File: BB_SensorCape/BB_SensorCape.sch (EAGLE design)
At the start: 15 parts, among them U1 FGPMMOPA6H

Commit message: schematic updates 12/23
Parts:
- removed B1: CR1220, microbuilder:BATTERYCR1220_SMT
- added C2: 0.1uF, SparkFun-Capacitors:0.1UF-25V-5%(0603)
- added C5, C6, C7, C8, C9: 0.1 uF, SparkFun-Capacitors:CAP0805
- added JP1: M02PTH, SparkFun-Connectors:M02PTH
- added JP2, JP3: (no value), adafruit:PINHD-2X4
- added PCB1: BEAGLEBONE_BLACK, e14_BeagleBoneBlack_RevA:BEAGLEBONE_BLACK
- added R10, R11, R12: 4.75K, resistor:R-US_R0603
- added R13: 10K, resistor:R-US_R0603
- added R14, R15, R5, R9: 5.6K, resistor:R-US_R0603
- added SW1: (no value), SparkFun-Electromechanical:SW_DIP-2-SMT-HALFSIZE
- added U$9: ISL29125, SparkFun-Sensors:ISL29125
- added U2: MAX232SOIC16, SparkFun-DigitalIC:MAX232SOIC16
- added X1: (no value), SparkFun-Connectors:DB9MALE
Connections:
- removed net I2C_SCL: R3.1, U$1.I2C1_SCL
- removed net I2C_SDA: R4.1, U$1.I2C1_SDA
- removed net VBACKUP: B1.+, U1.VBACKUP
- new net BB_GPS_RX: JP2.7, U$1.UART1_RXD
- new net BB_GPS_TX: JP2.3, U$1.UART1_TXD
- new net DBG_RX: U$1.UART2_RXD
- new net DBG_TX: U$1.UART2_TXD
- new net I2C2_SCL: R3.1, R5.1, U$1.I2C2_SCL, U$4.SCL
- new net I2C2_SDA: R4.1, R9.1, U$1.I2C2_SDA, U$4.SDA
- new net N$10: C7.1, U2.V-
- new net N$11: R11.1, SW1.1, U$4.A1
- new net N$12: R10.1, U$4.A2
- new net N$13: JP1.2, R13.1, U$4.WP
- new net N$14: C5.2, U2.C1-
- new net N$23: C8.1, U2.V+
- new net N$24: C5.1, U2.C1+
- new net N$27: C6.1, U2.C2+
- new net N$28: C6.2, U2.C2-
- new net N$9: R12.1, SW1.2, U$4.A0
- new net RXD: JP2.1, U2.R1OUT
- new net RXD#: U2.R1IN, X1.3
- new net TXD: JP2.5, U2.T1IN
- new net TXD#: U2.T1OUT, X1.2
- net 3.3V: now also C2.1, C9.1, R10.2, R11.2, R12.2, R5.2, R9.2, U$4.VCC, U2.VCC
- net GND: now also C2.2, C7.2, C8.2, C9.2, JP1.1, SW1.3, SW1.4, U$4.GND, U2.GND, U2.R2IN, U2.T2IN, X1.5; no longer B1.-
- net GPS_RX: now also JP2.2, JP2.4, U1.RX; no longer U$1.UART1_RXD, U1.TX
- net GPS_TX: now also JP2.6, JP2.8, U1.TX; no longer U$1.UART1_TXD, U1.RX
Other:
- note added: "Board Dimensions: 0.6" x 0.8""
- note added: "Board Dimensions: 1.5" x 0.9""
- note added: "I2C Address Range: 0x54 - 0x57"
- note added: "I2C Address: 0x44"
- note added: "Pin compatible with MAX3232E (3.3V Part)."
- note added: "Set Jumpers 1-2 and 5-6 for Serial Port-to-GPS Set Jumpers 3-4 and 7-8 for Beaglebone-to-GPS"
- note added: "Set Jumpers 3-4 and 7-8 for Beaglebone-to-Serial Port Only Install if Jumpers 3-4 and 7-8 are set on JP2"
- note added: "Shunt jumper enables EEPROM write."
- note added: "Use Digikey Part No. A35105-ND (Male Version) Confirm PCB footprint is for female (pins will need to be reversed on schematic if that's the case)"
- note added: "VERIFY SERIAL PORT JUMPER WIRING"
- note removed: "ADD SERIAL PORT COM"
- moved on the sheet: C1, LED2, R1, R2, R3, R4, R6, R7, R8, U$1, U$2, U$4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

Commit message: updates 12/24
added ISL29125 and started PWB design for area study
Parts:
- added C3: 1uF, SparkFun-Capacitors:CAP0805
- added C4: 0.1uF, SparkFun-Capacitors:0.1UF-25V-5%(0603)
- added R16: 10K, resistor:R-US_R0603
- added R17: 100, resistor:R-US_R0603
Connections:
- removed net FIX: LED2.A, U1.3D-FIX
- new net GPS_FIX: LED2.A, U$1.GPIO2_6, U1.3D-FIX
- new net ISL29125_INT: R16.1, U$1.GPIO2_9, U$9.!INT
- new net N$15: R14.1, U$9.SDA
- new net N$16: R15.1, U$9.SCL
- new net N$18: C3.1, C4.1, R17.1, U$9.VDD
- net 3.3V: now also PCB1.P9.3, PCB1.P9.4, R14.2, R15.2, R16.2, R17.2
- net 5V: now also PCB1.P9.5, PCB1.P9.6
- net DBG_RX: now also JP3.7
- net DBG_TX: now also JP3.3
- net GND: now also C3.2, C4.2, PCB1.P8.1, PCB1.P8.2, PCB1.P9.1, PCB1.P9.2, PCB1.P9.43, PCB1.P9.44, PCB1.P9.45, PCB1.P9.46, U$9.GND
- net RXD: now also JP3.8
- net TXD: now also JP3.4
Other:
- note added: "CALCULATE TOTAL CURRENT DRAW"
- note added: "I2C Addresses: 0x19, 0x1E, 0x6B, and 0x77"
- note removed: "ADD AMBIENT LIGHT SENSOR"
- note removed: "Wire FIX to GPIO?"
- moved on the sheet: C5, C6, C7, C8, C9, JP2, JP3, U2, X1

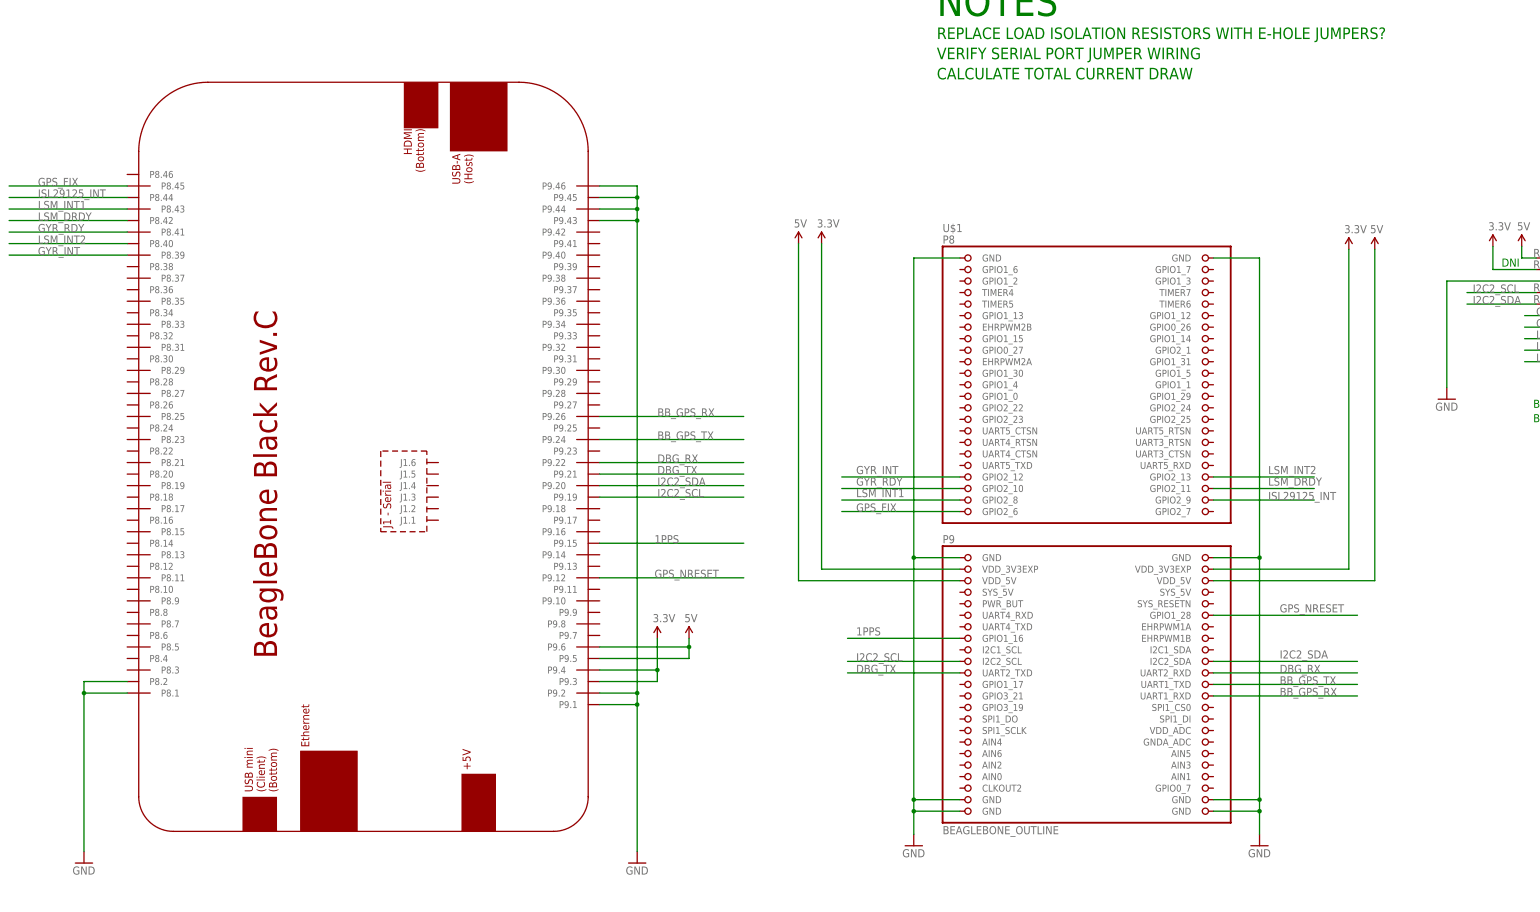
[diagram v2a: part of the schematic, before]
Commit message: Schematic/Board updates 01/03
Minor updates over holiday break
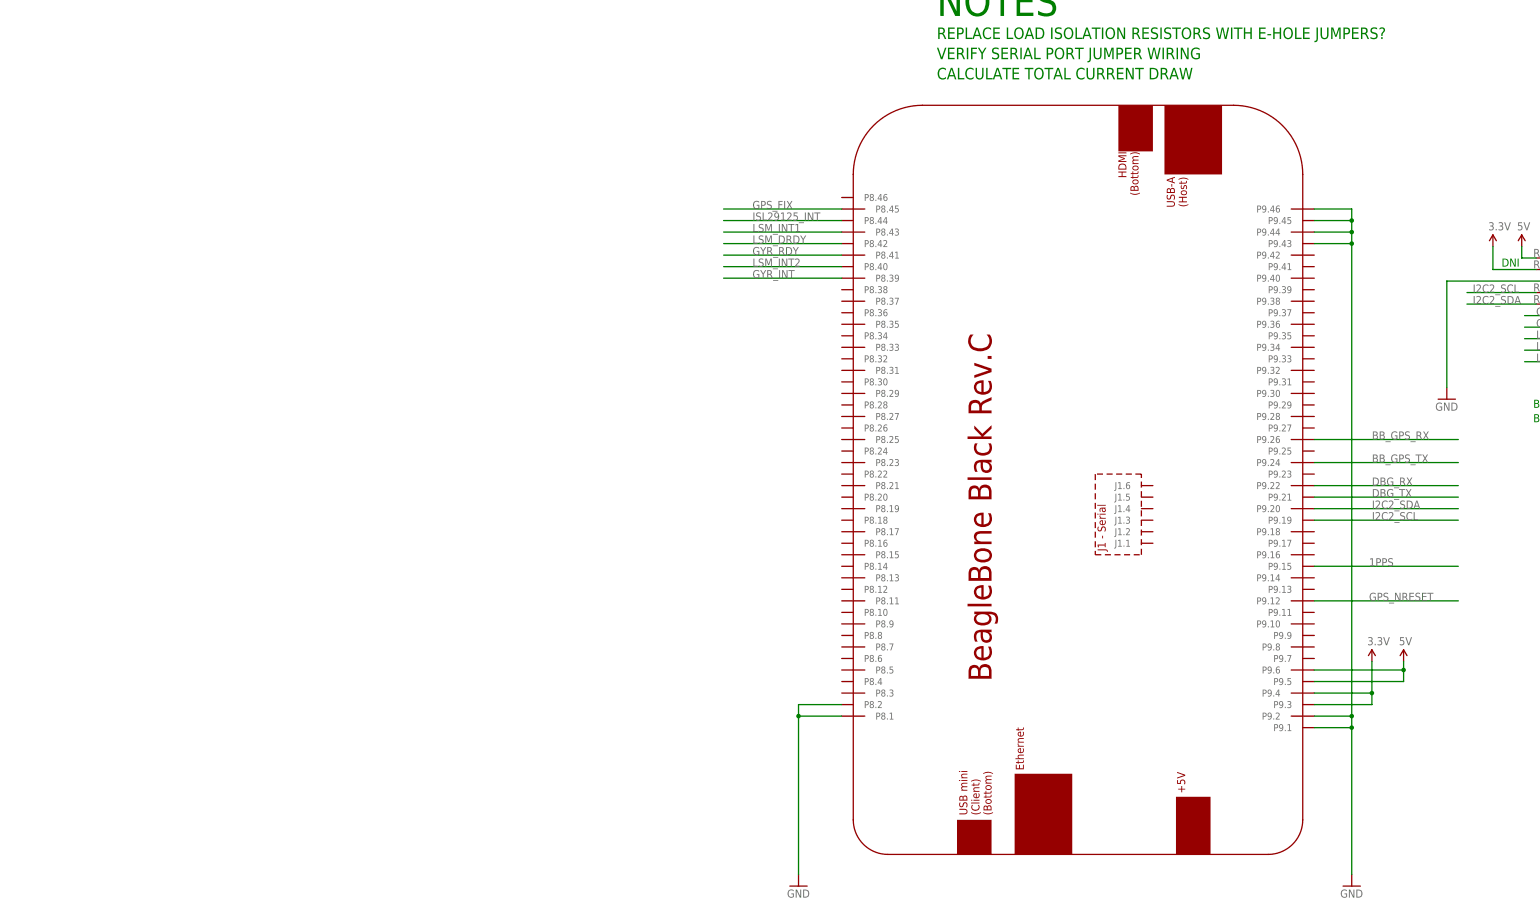
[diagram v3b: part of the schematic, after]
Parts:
- removed U$1: BEAGLEBONE_OUTLINE, adafruit:BEAGLEBONE_OUTLINE
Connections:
- net 1PPS: now also PCB1.P9.15; no longer U$1.GPIO1_16
- net 3.3V: no longer U$1.VDD_3V3EXP@1, U$1.VDD_3V3EXP@2
- net 5V: no longer U$1.VDD_5V@1, U$1.VDD_5V@2
- net BB_GPS_RX: now also PCB1.P9.26; no longer U$1.UART1_RXD
- net BB_GPS_TX: now also PCB1.P9.24; no longer U$1.UART1_TXD
- net DBG_RX: now also PCB1.P9.22; no longer U$1.UART2_RXD
- net DBG_TX: now also PCB1.P9.21; no longer U$1.UART2_TXD
- net GND: no longer U$1.GND@1, U$1.GND@2, U$1.GND@3, U$1.GND@4, U$1.GND@5, U$1.GND@6, U$1.GND@7, U$1.GND@8
- net GPS_FIX: now also PCB1.P8.45; no longer U$1.GPIO2_6
- net GPS_NRESET: now also PCB1.P9.12; no longer U$1.GPIO1_28
- net GYR_INT: now also PCB1.P8.39; no longer U$1.GPIO2_12
- net GYR_RDY: now also PCB1.P8.41; no longer U$1.GPIO2_10
- net I2C2_SCL: now also PCB1.P9.19; no longer U$1.I2C2_SCL
- net I2C2_SDA: now also PCB1.P9.20; no longer U$1.I2C2_SDA
- net ISL29125_INT: now also PCB1.P8.44; no longer U$1.GPIO2_9
- net LSM_DRDY: now also PCB1.P8.42; no longer U$1.GPIO2_11
- net LSM_INT1: now also PCB1.P8.43; no longer U$1.GPIO2_8
- net LSM_INT2: now also PCB1.P8.40; no longer U$1.GPIO2_13

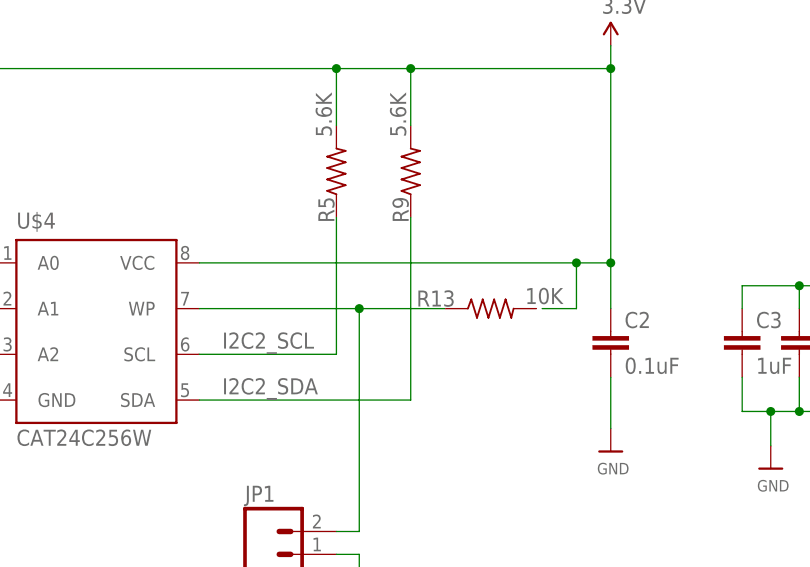
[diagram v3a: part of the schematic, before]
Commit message: Board updates 01/04
routing at ~98%
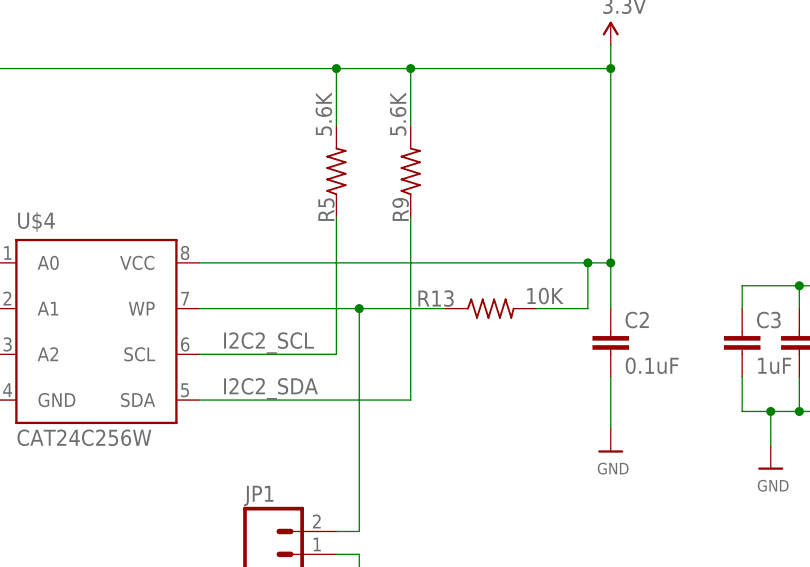
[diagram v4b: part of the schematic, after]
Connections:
- net 3.3V: now also R13.2
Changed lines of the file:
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@@
 <setting verticaltext="up"/>
 </settings>
-<grid distance="0.1" unitdist="inch" unit="inch" style="lines" multiple="1" display="no" altdistance="0.01" altunitdist="inch" altunit="inch"/>
+<grid distance="0.1" unitdist="inch" unit="inch" style="lines" multiple="1" display="yes" altdistance="0.01" altunitdist="inch" altunit="inch"/>
 <layers>
 <layer number="1" name="Top" color="4" fill="1" visible="no" active="no"/>
@@
 <wire x1="363.22" y1="127" x2="363.22" y2="132.08" width="0.1524" layer="91"/>
 <pinref part="U$4" gate="G$1" pin="VCC"/>
-<wire x1="363.22" y1="132.08" x2="359.41" y2="132.08" width="0.1524" layer="91"/>
 <pinref part="SUPPLY8" gate="G$1" pin="3.3V"/>
-<wire x1="359.41" y1="132.08" x2="317.5" y2="132.08" width="0.1524" layer="91"/>
+<wire x1="363.22" y1="132.08" x2="360.68" y2="132.08" width="0.1524" layer="91"/>
+<wire x1="360.68" y1="132.08" x2="317.5" y2="132.08" width="0.1524" layer="91"/>
 <wire x1="363.22" y1="132.08" x2="363.22" y2="153.67" width="0.1524" layer="91"/>
 <junction x="363.22" y="132.08"/>
@@
 <wire x1="277.495" y1="153.67" x2="283.21" y2="153.67" width="0.1524" layer="91"/>
 <junction x="283.21" y="153.67"/>
-<wire x1="355.6" y1="127" x2="359.41" y2="127" width="0.1524" layer="91"/>
-<wire x1="359.41" y1="127" x2="359.41" y2="132.08" width="0.1524" layer="91"/>
-<junction x="359.41" y="132.08"/>
+<wire x1="360.68" y1="132.08" x2="360.68" y2="127" width="0.1524" layer="91"/>
+<junction x="360.68" y="132.08"/>
+<wire x1="360.68" y1="127" x2="354.965" y2="127" width="0.1524" layer="91"/>
+<pinref part="R13" gate="G$1" pin="2"/>
 </segment>
 <segment>

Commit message: Schematic changes 02/03
Moved to FTDI interface for serial console
Refined jumper selection for serial console
Using TSL2561 BoB for ambient light sensor
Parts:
- removed C3: 1uF, SparkFun-Capacitors:CAP0805
- removed C4: 0.1uF, SparkFun-Capacitors:0.1UF-25V-5%(0603)
- removed C5, C6, C7, C8, C9: 0.1 uF, SparkFun-Capacitors:CAP0805
- removed U$9: ISL29125, SparkFun-Sensors:ISL29125
- removed U2: MAX232SOIC16, SparkFun-DigitalIC:MAX232SOIC16
- removed X1: (no value), SparkFun-Connectors:DB9MALE
- added JP4: FTDI_BASICPTH, SparkFun-Connectors:FTDI_BASICPTH
- added JP5: (no value), SparkFun-Connectors:M07
- added R18, R19: 4.75K, resistor:R-US_R0603
- added R20, R21: 0, resistor:R-US_R0603
- JP2: device adafruit:PINHD-2X4 -> jumper:JP4Q
- JP3: device adafruit:PINHD-2X4 -> jumper:JP2Q
- R14: value 5.6K -> 10K
- R15: value 5.6K -> 1K
- R16: value 10K -> 1K
- R17: value 100 -> 0
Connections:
- removed net N$18: C3.1, C4.1, R17.1, U$9.VDD
- removed net N$23: C8.1, U2.V+
- removed net N$24: C5.1, U2.C1+
- removed net N$27: C6.1, U2.C2+
- removed net N$28: C6.2, U2.C2-
- removed net RXD: JP2.1, JP3.8, U2.R1OUT
- removed net RXD#: U2.R1IN, X1.3
- removed net TXD: JP2.5, JP3.4, U2.T1IN
- removed net TXD#: U2.T1OUT, X1.2
- new net FTDI_RXD: JP2.2, JP3.3, JP4.2
- new net FTDI_TXD: JP2.6, JP3.1, JP4.3
- new net TSL2561_INT: JP5.5, PCB1.P8.46, R14.1
- net 3.3V: now also JP5.3, R18.2, R19.2, R21.2; no longer C9.1, R15.2, R17.2, U2.VCC
- net BB_GPS_RX: now also JP2.4, R18.1; no longer JP2.7
- net BB_GPS_TX: now also JP2.8; no longer JP2.3
- net DBG_RX: now also JP3.2, R19.1; no longer JP3.7
- net DBG_TX: now also JP3.4; no longer JP3.3
- net GND: now also JP4.6, JP5.2, R15.1; no longer C3.2, C4.2, C7.2, C8.2, C9.2, U$9.GND, U2.GND, U2.R2IN, U2.T2IN, X1.5
- net GPS_RX: now also JP2.5, JP2.7; no longer JP2.2, JP2.4
- net GPS_TX: now also JP2.1, JP2.3; no longer JP2.6, JP2.8
- net I2C2_SCL: now also R20.1
- net I2C2_SDA: now also R17.1
- net ISL29125_INT: no longer R16.1, U$9.!INT
- net N$10: now also JP5.4, R15.2, R16.1; no longer C7.1, U2.V-
- net N$14: now also JP5.7, R20.2; no longer C5.2, U2.C1-
- net N$15: now also JP5.6, R17.2; no longer R14.1, U$9.SDA
- net N$16: now also JP5.1, R21.1; no longer R15.1, U$9.SCL
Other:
- note added: "Adafruit TSL2561 Breakout"
- note added: "I2C Addresses: ADDR grounded = 0x29 ADDR floating = 0x39 ADDR pulled up = 0x49"
- note added: "Look at I2C Pullup Distribution"
- note added: "Set Jumpers 1-2 and 3-4 for Beaglebone-to-Debug Port Only valid if Jumpers 1-2 and 5-6 aren't installed on JP2"
- note added: "Set Jumpers 3-4 and 7-8 for Beaglebone-to-GPS Set Jumpers 1-2 and 5-6 for Debug Port-to-GPS"
- note removed: "I2C Address: 0x44"
- note removed: "Pin compatible with MAX3232E (3.3V Part)."
- note removed: "REPLACE LOAD ISOLATION RESISTORS WITH E-HOLE JUMPERS?"
- note removed: "Set Jumpers 1-2 and 5-6 for Serial Port-to-GPS Set Jumpers 3-4 and 7-8 for Beaglebone-to-GPS"
- note removed: "Set Jumpers 3-4 and 7-8 for Beaglebone-to-Serial Port Only Install if Jumpers 3-4 and 7-8 are set on JP2"
- note removed: "Use Digikey Part No. A35105-ND (Male Version) Confirm PCB footprint is for female (pins will need to be reversed on schematic if that's the case)"
- moved on the sheet: C1, C2, JP1, LED2, R1, R10, R11, R12, R13, R14, R15, R16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
